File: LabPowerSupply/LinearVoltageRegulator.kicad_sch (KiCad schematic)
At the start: 15 parts, among them Q1_LVR1 PJA3404_R1_00001, Q2_LVR1 PJA3404_R1_00001, Q3_LVR1 PJA3404_R1_00001

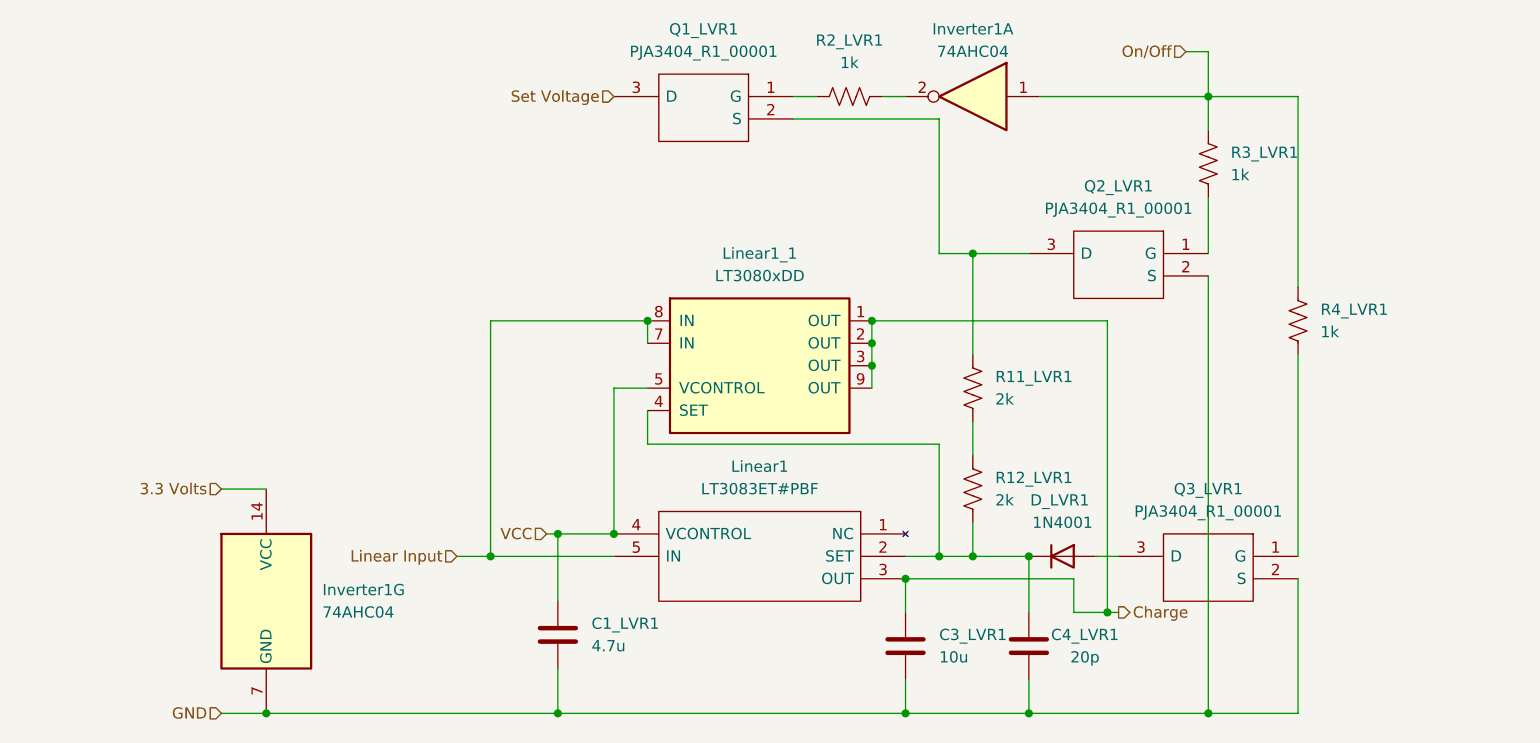
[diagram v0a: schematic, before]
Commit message: Finished grouping regulation parts
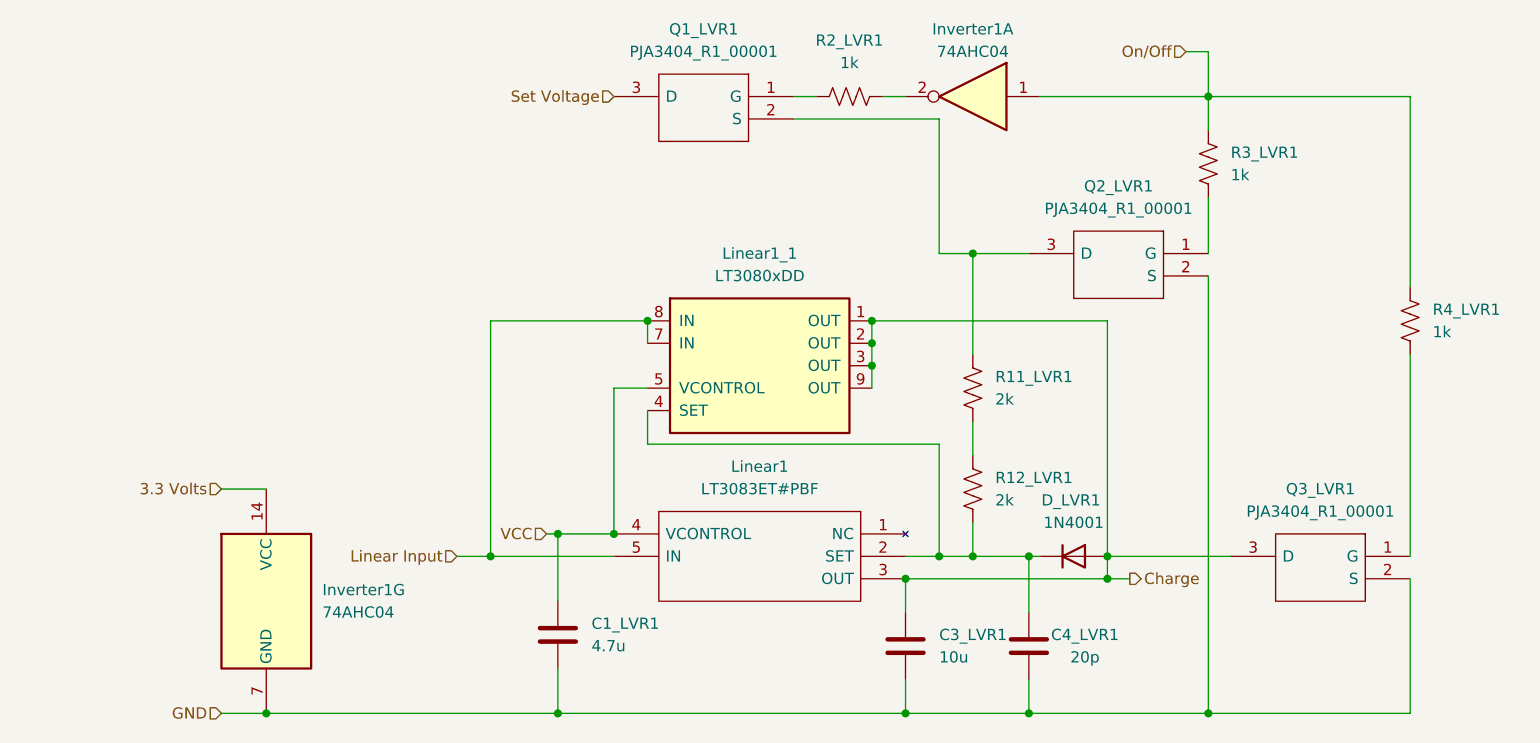
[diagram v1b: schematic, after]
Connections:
- net Charge: now also D_LVR1.2 (A), Q3_LVR1.3 (D)
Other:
- moved on the sheet: D_LVR1, Q3_LVR1, R4_LVR1

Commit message: Squeezed main regulator
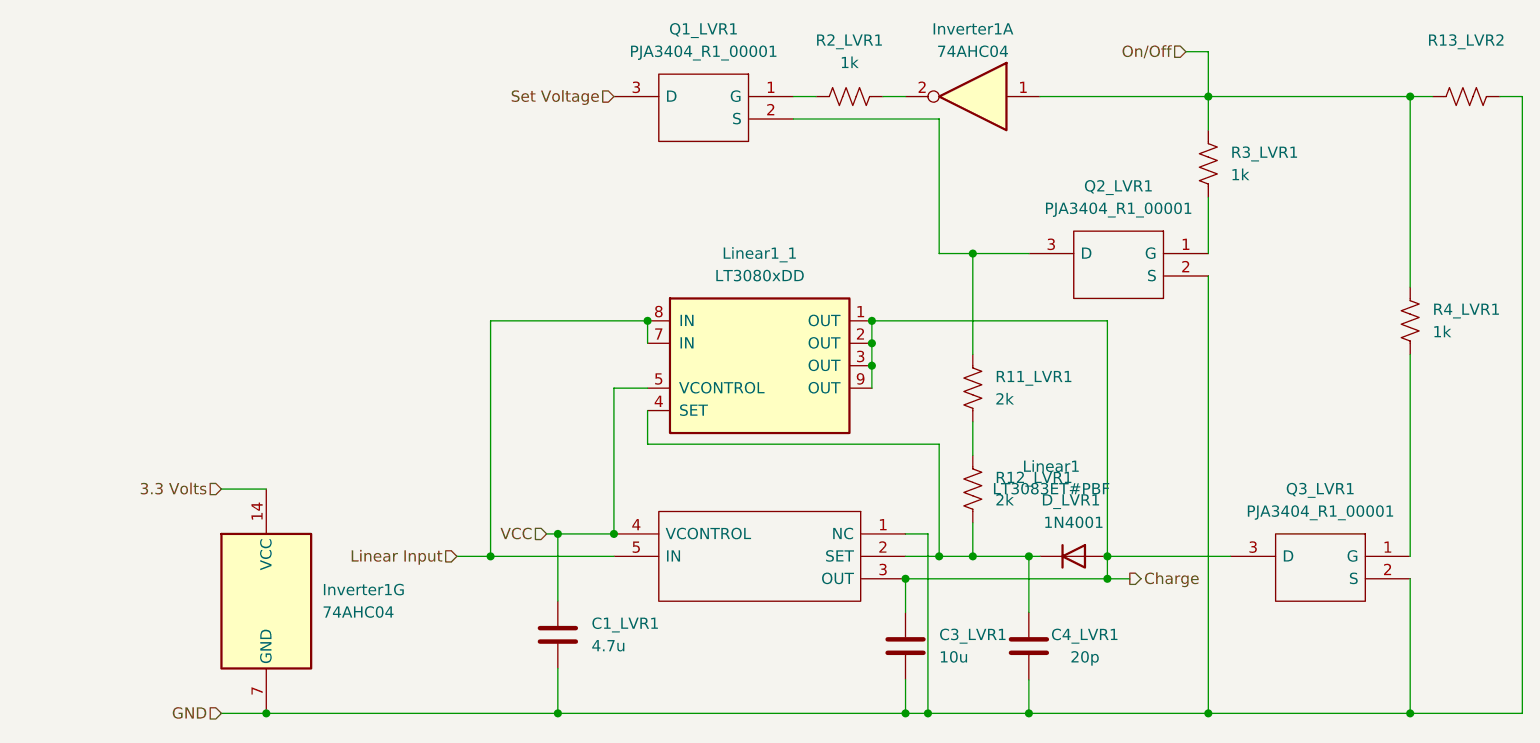
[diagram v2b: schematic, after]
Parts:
- added R13_LVR2: (no value), Resistor_SMD:R_0603_1608Metric, symbol Device:R_US
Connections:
- net GND: now also Linear1.1 (NC), R13_LVR2.1
- net On/Off: now also R13_LVR2.2
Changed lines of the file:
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@@
     (comment 4 "The linear voltage regulator is the main source for the power")
   )
+  (junction (at 227.33 139.7) (diameter 0) (color 0 0 0 0)
+  )
+  (junction (at 172.72 139.7) (diameter 0) (color 0 0 0 0)
+  )
   (junction (at 177.8 87.63) (diameter 0) (color 0 0 0 0)
   )
@@
   (junction (at 170.18 139.7) (diameter 0) (color 0 0 0 0)
   )
+  (junction (at 227.33 69.85) (diameter 0) (color 0 0 0 0)
+  )
   (junction (at 204.47 139.7) (diameter 0) (color 0 0 0 0)
   )
@@
     (stroke (width 0) (type default) (color 0 0 0 0))
   )
+  (wire (pts (xy 170.18 119.38) (xy 172.72 119.38))
+    (stroke (width 0) (type default) (color 0 0 0 0))
+  )
   (wire (pts (xy 170.18 121.92) (xy 173.99 121.92))
     (stroke (width 0) (type default) (color 0 0 0 0))
@@
     (stroke (width 0) (type default) (color 0 0 0 0))
   )
-  (wire (pts (xy 170.18 139.7) (xy 184.15 139.7))
+  (wire (pts (xy 240.03 69.85) (xy 237.49 69.85))
+    (stroke (width 0) (type default) (color 0 0 0 0))
+  )
+  (wire (pts (xy 170.18 139.7) (xy 172.72 139.7))
     (stroke (width 0) (type default) (color 0 0 0 0))
   )
@@
     (stroke (width 0) (type default) (color 0 0 0 0))
   )
+  (wire (pts (xy 172.72 139.7) (xy 184.15 139.7))
+    (stroke (width 0) (type default) (color 0 0 0 0))
+  )
   (wire (pts (xy 184.15 128.27) (xy 184.15 121.92))
     (stroke (width 0) (type default) (color 0 0 0 0))
@@
     (stroke (width 0) (type default) (color 0 0 0 0))
   )
+  (wire (pts (xy 240.03 139.7) (xy 227.33 139.7))
+    (stroke (width 0) (type default) (color 0 0 0 0))
+  )
   (wire (pts (xy 201.93 64.77) (xy 204.47 64.77))
     (stroke (width 0) (type default) (color 0 0 0 0))
@@
     (stroke (width 0) (type default) (color 0 0 0 0))
   )
+  (wire (pts (xy 229.87 69.85) (xy 227.33 69.85))
+    (stroke (width 0) (type default) (color 0 0 0 0))
+  )
   (wire (pts (xy 204.47 139.7) (xy 227.33 139.7))
     (stroke (width 0) (type default) (color 0 0 0 0))
@@
     (stroke (width 0) (type default) (color 0 0 0 0))
   )
+  (wire (pts (xy 240.03 69.85) (xy 240.03 139.7))
+    (stroke (width 0) (type default) (color 0 0 0 0))
+  )
   (wire (pts (xy 173.99 72.39) (xy 173.99 87.63))
     (stroke (width 0) (type default) (color 0 0 0 0))
@@
   )
   (wire (pts (xy 166.37 97.79) (xy 166.37 100.33))
+    (stroke (width 0) (type default) (color 0 0 0 0))
+  )
+  (wire (pts (xy 172.72 119.38) (xy 172.72 139.7))
     (stroke (width 0) (type default) (color 0 0 0 0))
   )
@@
   (symbol (lib_id "SamacSys_Parts:LT3083ET#PBF") (at 170.18 119.38 0) (mirror y) (unit 1)
     (in_bom yes) (on_board yes) (fields_autoplaced)
-    (property "Reference" "Linear1" (id 0) (at 153.67 111.76 0))
-    (property "Value" "LT3083ET#PBF" (id 1) (at 153.67 114.3 0))
-    (property "Footprint" "SamacSys_Parts:TO170P457X1022X2306-5P" (id 2) (at 140.97 116.84 0)
-      (effects (font (size 1.27 1.27)) (justify left) hide)
-    )
-    (property "Datasheet" "http://www.linear.com/docs/30239" (id 3) (at 140.97 119.38 0)
-      (effects (font (size 1.27 1.27)) (justify left) hide)
-    )
-    (property "Description" "IC REG LDO ADJ 3A TO220-5" (id 4) (at 140.97 121.92 0)
-      (effects (font (size 1.27 1.27)) (justify left) hide)
-    )
-    (property "Height" "4.572" (id 5) (at 140.97 124.46 0)
-      (effects (font (size 1.27 1.27)) (justify left) hide)
-    )
-    (property "Mouser Part Number" "584-LT3083ET#PBF" (id 6) (at 140.97 127 0)
-      (effects (font (size 1.27 1.27)) (justify left) hide)
-    )
-    (property "Mouser Price/Stock" "https://www.mouser.co.uk/ProductDetail/Analog-Devices/LT3083ETPBF?qs=hVkxg5c3xu%252BEQibxnmC0QQ%3D%3D" (id 7) (at 140.97 129.54 0)
-      (effects (font (size 1.27 1.27)) (justify left) hide)
-    )
-    (property "Manufacturer_Name" "Analog Devices" (id 8) (at 140.97 132.08 0)
-      (effects (font (size 1.27 1.27)) (justify left) hide)
-    )
-    (property "Manufacturer_Part_Number" "LT3083ET#PBF" (id 9) (at 140.97 134.62 0)
+    (property "Reference" "Linear1" (id 0) (at 186.69 111.76 0))
+    (property "Value" "LT3083ET#PBF" (id 1) (at 186.69 114.3 0))
+    (property "Footprint" "SamacSys_Parts:TO170P457X1022X2306-5P" (id 2) (at 199.39 116.84 0)
+      (effects (font (size 1.27 1.27)) (justify left) hide)
+    )
+    (property "Datasheet" "http://www.linear.com/docs/30239" (id 3) (at 210.82 107.95 0)
+      (effects (font (size 1.27 1.27)) (justify left) hide)
+    )
+    (property "Description" "IC REG LDO ADJ 3A TO220-5" (id 4) (at 199.39 121.92 0)
+      (effects (font (size 1.27 1.27)) (justify left) hide)
+    )
+    (property "Height" "4.572" (id 5) (at 199.39 124.46 0)
+      (effects (font (size 1.27 1.27)) (justify left) hide)
+    )
+    (property "Mouser Part Number" "584-LT3083ET#PBF" (id 6) (at 199.39 127 0)
+      (effects (font (size 1.27 1.27)) (justify left) hide)
+    )
+    (property "Mouser Price/Stock" "https://www.mouser.co.uk/ProductDetail/Analog-Devices/LT3083ETPBF?qs=hVkxg5c3xu%252BEQibxnmC0QQ%3D%3D" (id 7) (at 199.39 129.54 0)
+      (effects (font (size 1.27 1.27)) (justify left) hide)
+    )
+    (property "Manufacturer_Name" "Analog Devices" (id 8) (at 199.39 132.08 0)
+      (effects (font (size 1.27 1.27)) (justify left) hide)
+    )
+    (property "Manufacturer_Part_Number" "LT3083ET#PBF" (id 9) (at 199.39 134.62 0)
       (effects (font (size 1.27 1.27)) (justify left) hide)
     )
@@
       (effects (font (size 1.27 1.27)) hide)
     )
+    (pin "1")
+    (pin "2")
+  )
+  (symbol (lib_id "Device:R_US") (at 233.68 69.85 270) (unit 1)
+    (in_bom yes) (on_board yes) (fields_autoplaced)
+    (property "Reference" "R13_LVR2" (id 0) (at 233.68 63.5 90))
+    (property "Value" "" (id 1) (at 233.68 66.04 90))
+    (property "Footprint" "Resistor_SMD:R_0603_1608Metric" (id 2) (at 233.426 70.866 90)
+      (effects (font (size 1.27 1.27)) hide)
+    )
+    (property "Datasheet" "~" (id 3) (at 233.68 69.85 0)
+      (effects (font (size 1.27 1.27)) hide)
+    )

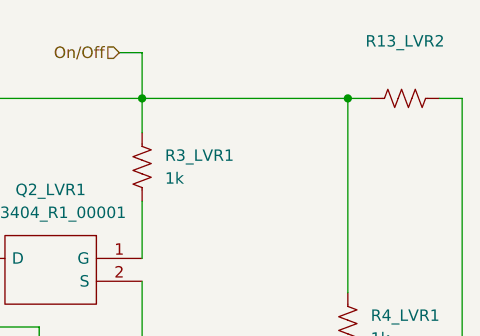
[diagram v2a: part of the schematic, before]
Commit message: Extended ground fill
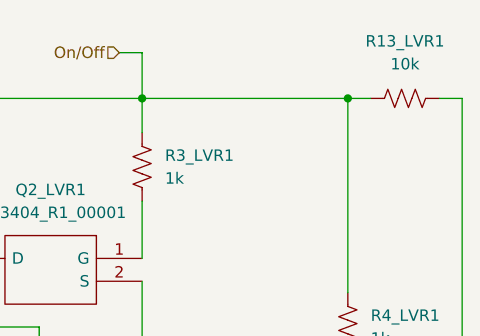
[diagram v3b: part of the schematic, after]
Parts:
- R13_LVR1: renamed from R13_LVR2; value (none) -> 10k
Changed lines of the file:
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@@
   (symbol (lib_id "Device:R_US") (at 233.68 69.85 270) (unit 1)
     (in_bom yes) (on_board yes) (fields_autoplaced)
-    (property "Reference" "R13_LVR2" (id 0) (at 233.68 63.5 90))
-    (property "Value" "" (id 1) (at 233.68 66.04 90))
+    (property "Reference" "R13_LVR1" (id 0) (at 233.68 63.5 90))
+    (property "Value" "10k" (id 1) (at 233.68 66.04 90))
     (property "Footprint" "Resistor_SMD:R_0603_1608Metric" (id 2) (at 233.426 70.866 90)
       (effects (font (size 1.27 1.27)) hide)

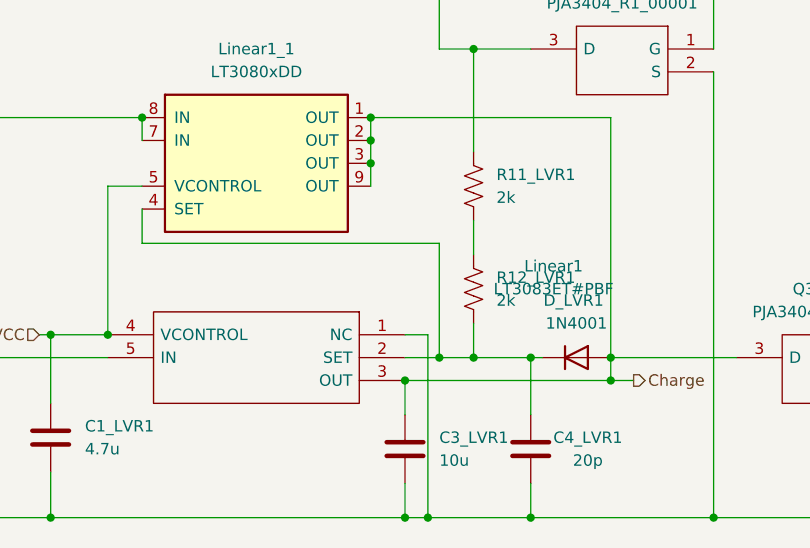
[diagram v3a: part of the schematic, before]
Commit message: Fixed MCU communication pins and optocoupler
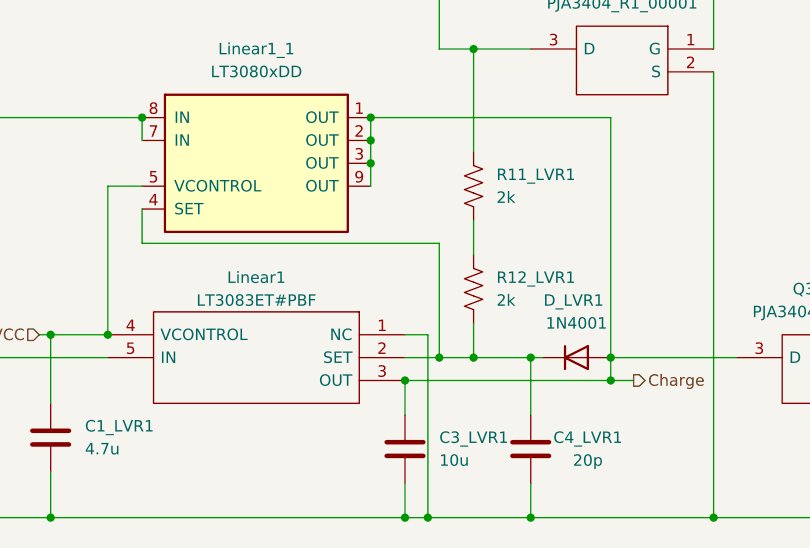
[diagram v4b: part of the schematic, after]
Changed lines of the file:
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@@
   )
   (symbol (lib_id "SamacSys_Parts:LT3083ET#PBF") (at 170.18 119.38 0) (mirror y) (unit 1)
-    (in_bom yes) (on_board yes) (fields_autoplaced)
-    (property "Reference" "Linear1" (id 0) (at 186.69 111.76 0))
-    (property "Value" "LT3083ET#PBF" (id 1) (at 186.69 114.3 0))
+    (in_bom yes) (on_board yes)
+    (property "Reference" "Linear1" (id 0) (at 153.67 113.03 0))
+    (property "Value" "LT3083ET#PBF" (id 1) (at 153.67 115.57 0))
     (property "Footprint" "SamacSys_Parts:TO170P457X1022X2306-5P" (id 2) (at 199.39 116.84 0)
       (effects (font (size 1.27 1.27)) (justify left) hide)

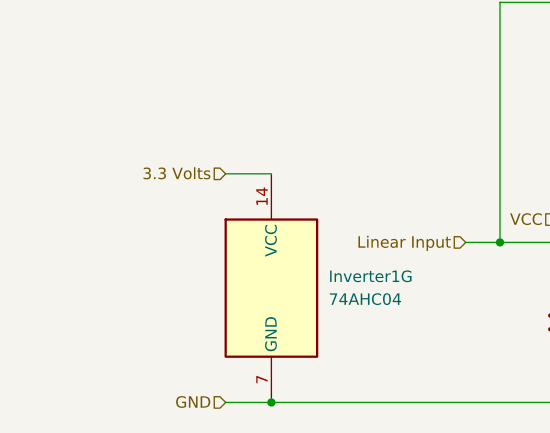
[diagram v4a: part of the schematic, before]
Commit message: Began mcu placement
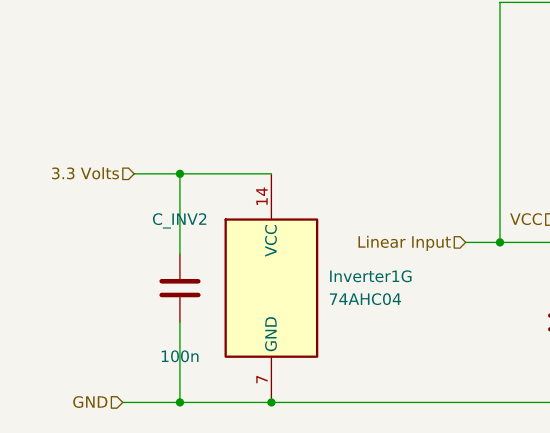
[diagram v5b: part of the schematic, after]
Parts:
- added C_INV2: 100n, Capacitor_SMD:C_0603_1608Metric, symbol Device:C
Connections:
- net 3.3 Volts: now also C_INV2.2
- net GND: now also C_INV2.1
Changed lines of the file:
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@@
   (junction (at 193.04 121.92) (diameter 0) (color 0 0 0 0)
   )
+  (junction (at 87.63 114.3) (diameter 0) (color 0 0 0 0)
+  )
   (junction (at 137.16 119.38) (diameter 0) (color 0 0 0 0)
   )
@@
   (junction (at 184.15 121.92) (diameter 0) (color 0 0 0 0)
   )
+  (junction (at 87.63 139.7) (diameter 0) (color 0 0 0 0)
+  )
   (junction (at 170.18 124.46) (diameter 0) (color 0 0 0 0)
   )
@@
     (stroke (width 0) (type default) (color 0 0 0 0))
   )
+  (wire (pts (xy 87.63 114.3) (xy 97.79 114.3))
+    (stroke (width 0) (type default) (color 0 0 0 0))
+  )
+  (wire (pts (xy 87.63 139.7) (xy 97.79 139.7))
+    (stroke (width 0) (type default) (color 0 0 0 0))
+  )
   (wire (pts (xy 173.99 109.22) (xy 173.99 121.92))
     (stroke (width 0) (type default) (color 0 0 0 0))
@@
     (stroke (width 0) (type default) (color 0 0 0 0))
   )
-  (wire (pts (xy 92.71 114.3) (xy 97.79 114.3))
+  (wire (pts (xy 82.55 114.3) (xy 87.63 114.3))
+    (stroke (width 0) (type default) (color 0 0 0 0))
+  )
+  (wire (pts (xy 87.63 130.81) (xy 87.63 139.7))
     (stroke (width 0) (type default) (color 0 0 0 0))
   )
@@
     (stroke (width 0) (type default) (color 0 0 0 0))
   )
+  (wire (pts (xy 87.63 114.3) (xy 87.63 123.19))
+    (stroke (width 0) (type default) (color 0 0 0 0))
+  )
   (wire (pts (xy 184.15 128.27) (xy 184.15 121.92))
     (stroke (width 0) (type default) (color 0 0 0 0))
@@
     (stroke (width 0) (type default) (color 0 0 0 0))
   )
-  (wire (pts (xy 92.71 139.7) (xy 97.79 139.7))
+  (wire (pts (xy 81.28 139.7) (xy 87.63 139.7))
     (stroke (width 0) (type default) (color 0 0 0 0))
   )
@@
     (effects (font (size 1.27 1.27)) (justify left))
   )
-  (hierarchical_label "3.3 Volts" (shape input) (at 92.71 114.3 180)
+  (hierarchical_label "3.3 Volts" (shape input) (at 82.55 114.3 180)
     (effects (font (size 1.27 1.27)) (justify right))
   )
-  (hierarchical_label "GND" (shape input) (at 92.71 139.7 180)
+  (hierarchical_label "GND" (shape input) (at 81.28 139.7 180)
     (effects (font (size 1.27 1.27)) (justify right))
   )
@@
       (effects (font (size 1.27 1.27)) hide)
     )
+    (pin "1")
+    (pin "2")
+  )
+  (symbol (lib_id "Device:C") (at 87.63 127 180) (unit 1)
+    (in_bom yes) (on_board yes)
+    (property "Reference" "C_INV2" (id 0) (at 87.63 119.38 0))
+    (property "Value" "100n" (id 1) (at 87.63 134.62 0))
+    (property "Footprint" "Capacitor_SMD:C_0603_1608Metric" (id 2) (at 86.6648 123.19 0)
+      (effects (font (size 1.27 1.27)) hide)
+    )
+    (property "Datasheet" "~" (id 3) (at 87.63 127 0)
+      (effects (font (size 1.27 1.27)) hide)
+    )

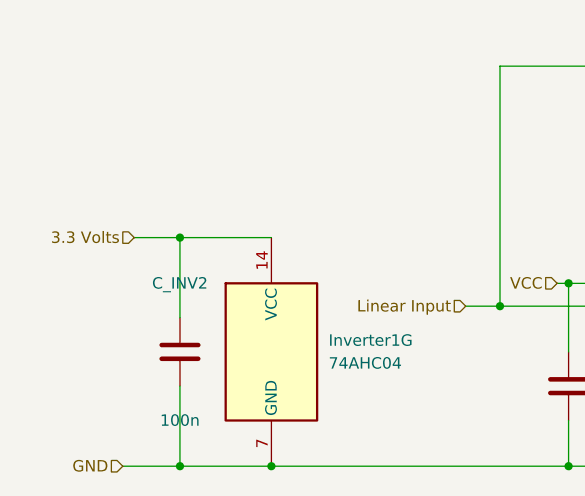
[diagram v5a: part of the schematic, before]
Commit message: Ch1 MCU placement
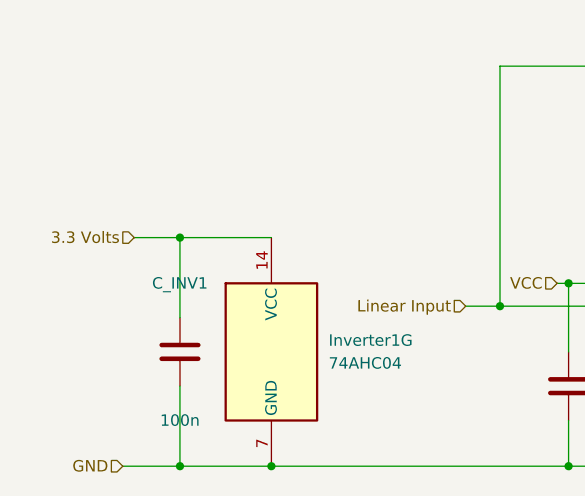
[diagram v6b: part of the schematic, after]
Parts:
- renumbered C_INV2 to C_INV1
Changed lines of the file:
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@@
   (symbol (lib_id "Device:C") (at 87.63 127 180) (unit 1)
     (in_bom yes) (on_board yes)
-    (property "Reference" "C_INV2" (id 0) (at 87.63 119.38 0))
+    (property "Reference" "C_INV1" (id 0) (at 87.63 119.38 0))
     (property "Value" "100n" (id 1) (at 87.63 134.62 0))
     (property "Footprint" "Capacitor_SMD:C_0603_1608Metric" (id 2) (at 86.6648 123.19 0)
